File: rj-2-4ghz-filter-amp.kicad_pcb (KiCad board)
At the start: 4 copper layers, 142.2 x 80.3 mm, 86 parts, among them IC1 MP1584EN-LF-Z, IC2 MP1584EN-LF-Z, J2 Barrel_Jack, J3 Conn_01x03, J4 Conn_01x03, J5 Conn_01x03, J6 Conn_01x03, J7 Conn_01x02, J8 Conn_01x02, J9 Conn_01x02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

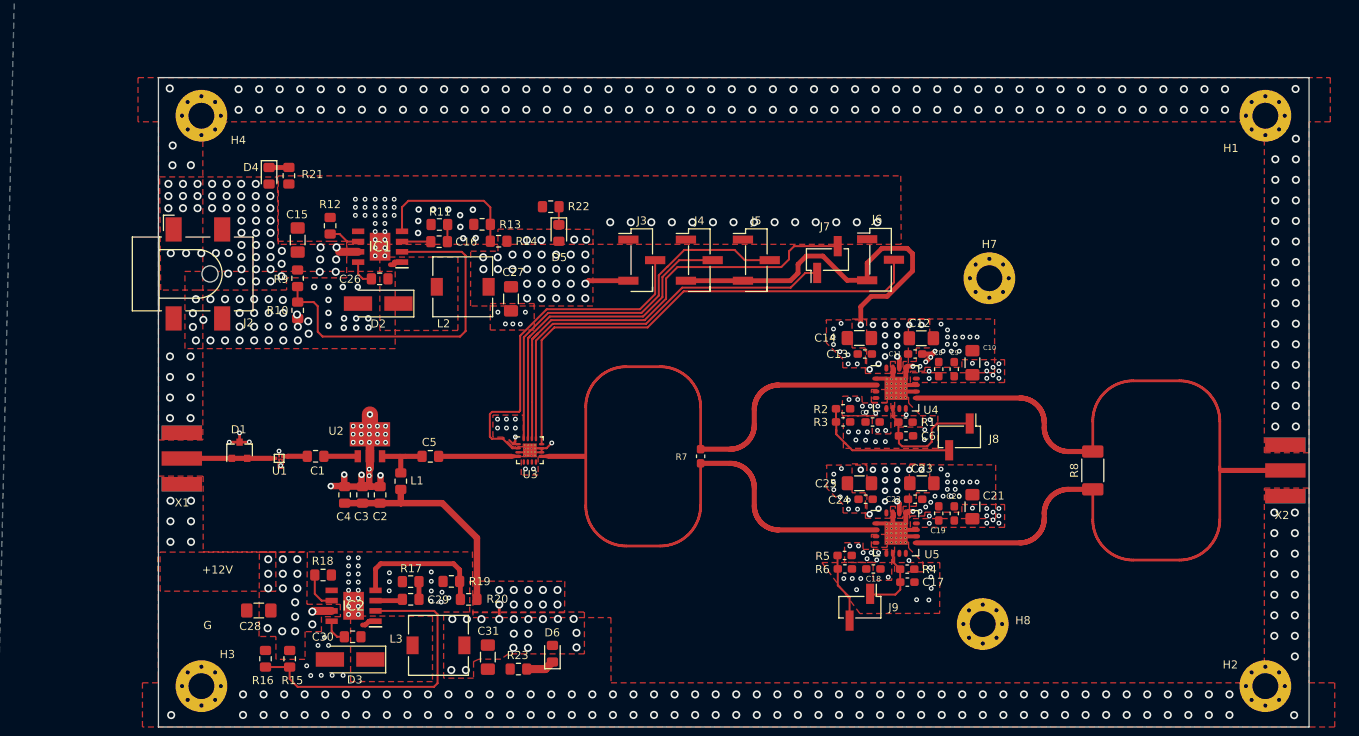
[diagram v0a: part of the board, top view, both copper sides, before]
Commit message: adds annotations
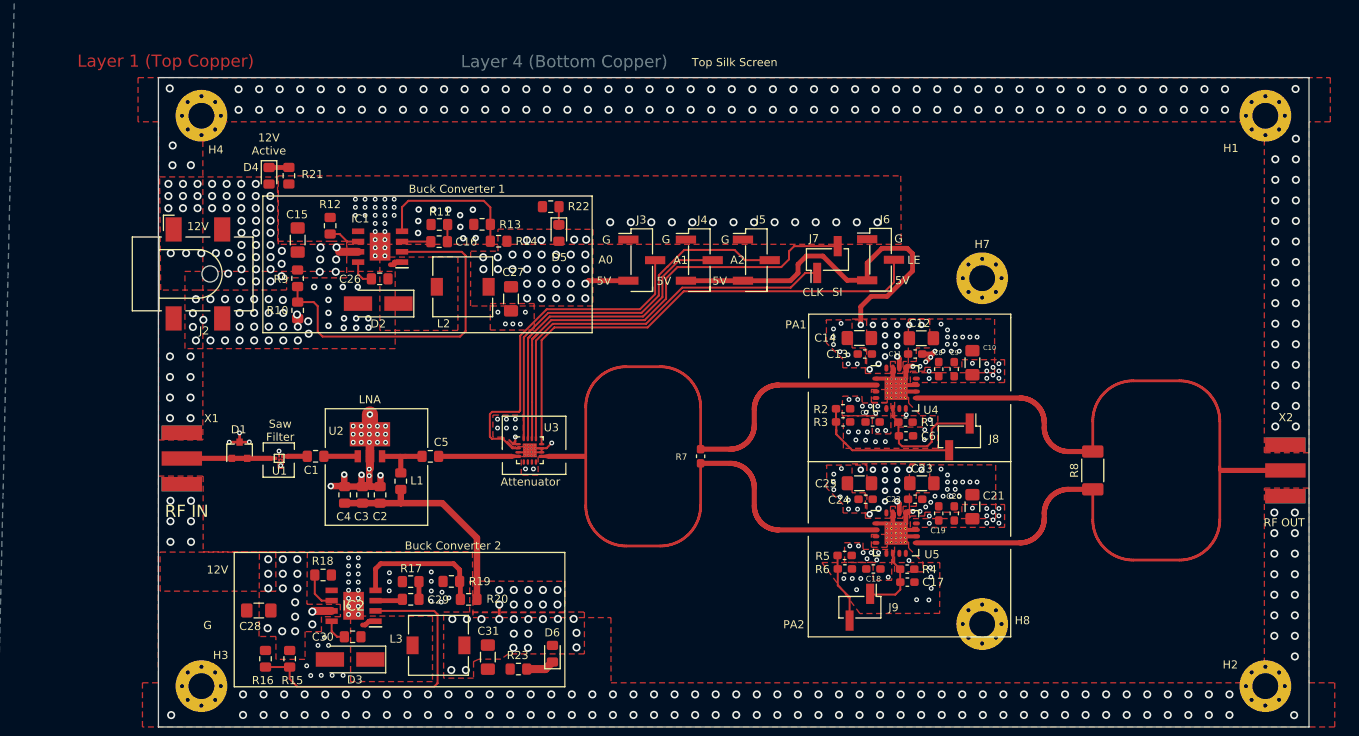
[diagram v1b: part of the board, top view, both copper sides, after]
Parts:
- moved H7 0.89 mm to (193.0, 68.1)
- moved H8 0.07 mm to (193.0, 110.8)
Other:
- board text added: "12V"
- board text added: "12V Active"
- board text added: "5V"
- board text added: "A0"
- board text added: "A1"
- board text added: "A2"
- board text added: "Attenuator"
- board text added: "Bottom Mask"
- board text added: "Bottom Silk Screen"
- board text added: "Bottom paste"
- board text added: "Buck Converter 1"
- board text added: "Buck Converter 2"
- board text added: "CLK"
- board text added: "Front Paste"
- board text added: "LE"
- board text added: "LNA"
- board text added: "Layer 1 (Top Copper)"
- board text added: "Layer 2"
- board text added: "Layer 3"
- board text added: "Layer 4 (Bottom Copper)"
- board text added: "PA1"
- board text added: "PA2"
- board text added: "RF IN"
- board text added: "RF OUT"
- board text added: "SI"
- board text added: "Saw Filter"
- board text added: "Top Mask"
- board text added: "Top Silk Screen"
- board text removed: "+12V"

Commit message: gerber and bom generated
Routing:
- net /5V_B1: track 56.2 -> 55.2 mm
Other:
- board text added: "*Keep J7 shorted to ground by default when not using serial communication"
- board text added: "D1 BAV99"
- board text added: "IC1, IC2 MP1584EN-LF-Z"
- board text added: "J3, J4, J5 Address pin for serial communication"
- board text added: "J6, J7 Serial comunication"
- board text added: "J8 Enable PA1"
- board text added: "J9 Enable PA2"
- board text added: "Kamui"
- board text added: "RadioJitter"
- board text added: "SAW Filter"
- board text added: "Tech"
- board text added: "U1 B39242B4360P810"
- board text added: "U2 SPF5189Z"
- board text added: "U3 RFSA3613"
- board text added: "U4, U5 SKY66295"
- board text removed: "Saw Filter"
